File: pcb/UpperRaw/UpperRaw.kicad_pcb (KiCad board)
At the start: 2 copper layers, 52 x 63 mm, 20 parts, among them J1 Conn_01x04, SW100 SW_DPDT_x2, SW101 SW_DPDT_x2, SW102 SW_SPDT, SW103 SW_SPDT

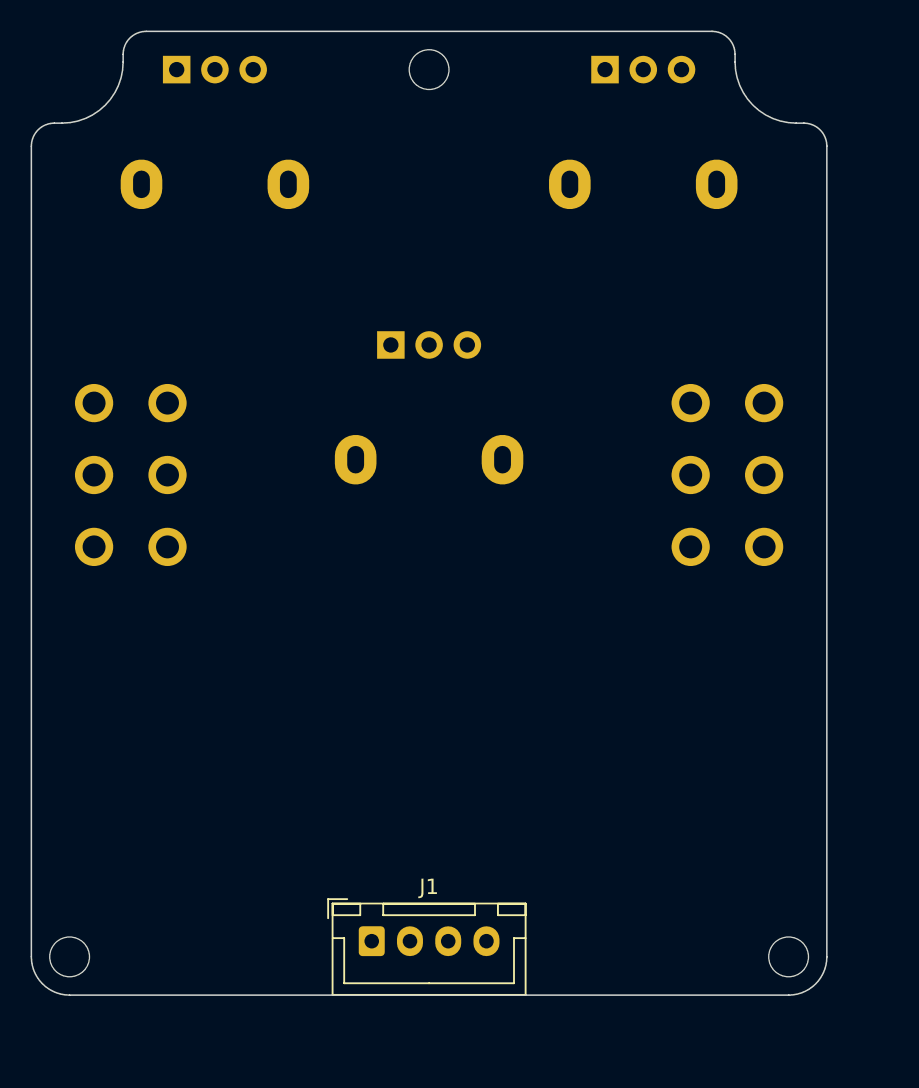
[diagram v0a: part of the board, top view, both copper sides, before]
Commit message: [UpperRaw] swap mounting holes for M3 ones
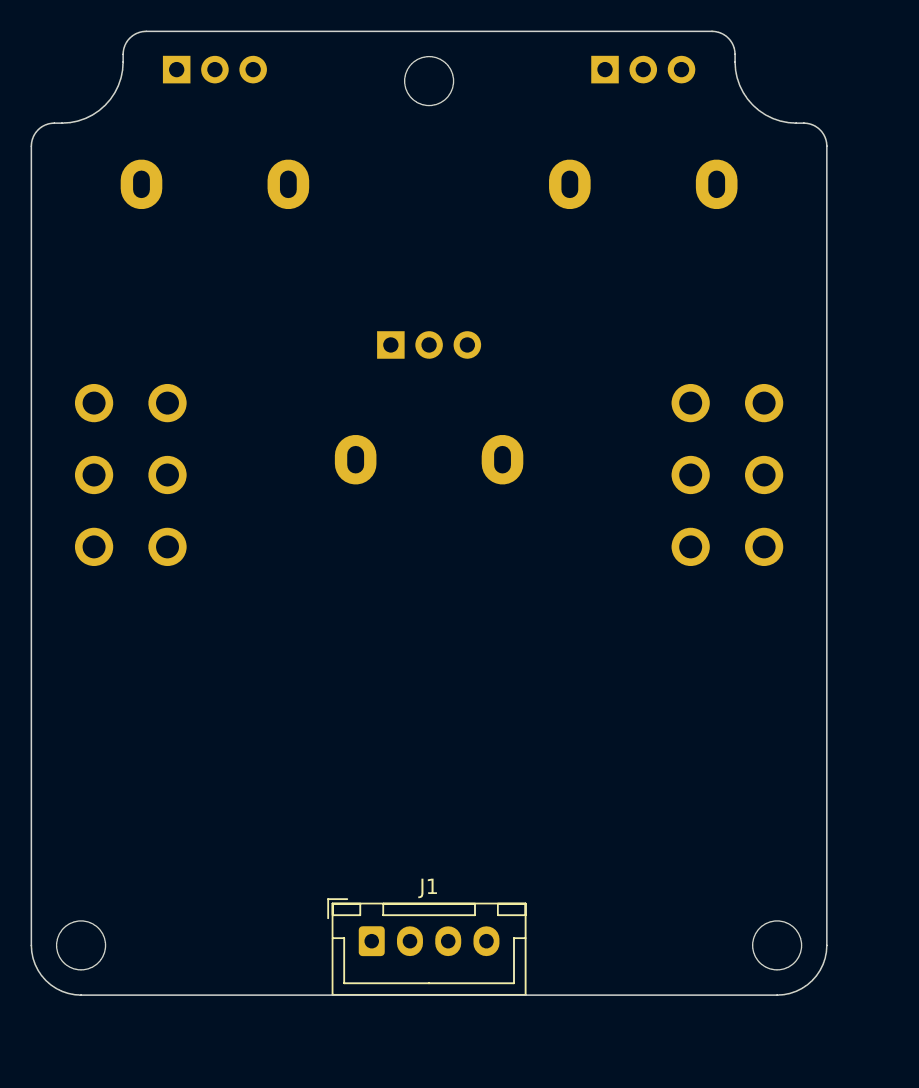
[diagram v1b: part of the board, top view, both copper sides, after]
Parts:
- removed the MK2 at (149.5, 70.0)
- removed the MK2 at (173.0, 128.0)
- removed the MK2 at (126.0, 128.0)
- added MK2: Mounting_Hole, MeineBib:EigenesMountingHole_3.2mm_M3_Small, F.Cu at (126.8, 127.2)
- added MK2: Mounting_Hole, MeineBib:EigenesMountingHole_3.2mm_M3_Small, F.Cu at (172.2, 127.2)
- added MK2: Mounting_Hole, MeineBib:EigenesMountingHole_3.2mm_M3_Small, F.Cu at (149.5, 70.8)
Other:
- outline, holes or cut-outs redrawn
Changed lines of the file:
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@@
+    )
+  )
+  (footprint "MeineBib:EigenesMountingHole_3.2mm_M3_Small" (layer "F.Cu")
+    (at 126.75 127.25)
+    (descr "Mounting Hole 2.7mm, no annular, M2.5")
+    (tags "mounting hole 2.7mm no annular m2.5")
+    (attr exclude_from_pos_files exclude_from_bom)
+    (fp_text reference "MK2" (at 0 -3.7) (layer "F.SilkS") hide
+      (effects (font (size 1 1) (thickness 0.15)))
+    )
+    (fp_text value "Mounting_Hole" (at 0 3.7) (layer "F.Fab")
+      (effects (font (size 1 1) (thickness 0.15)))
+    )
+    (fp_text user "${REFERENCE}" (at 0.3 0) (layer "F.Fab")
+      (effects (font (size 1 1) (thickness 0.15)))
+    )
+    (fp_circle (center 0 0) (end 3.1 0) (layer "Cmts.User") (width 0.15) (fill none))
+    (fp_circle (center 0 0) (end 3.1 0) (layer "F.CrtYd") (width 0.05) (fill none))
+    (pad "" np_thru_hole circle (at 0 0) (size 3.2 3.2) (drill 3.2) (layers F&B.Cu *.Mask)
+      (solder_mask_margin 1.65) (clearance 1.8))
+    (model "${MEINE_BIBS}/MeineBib.3dshapes/m3standoffs/M3x6-Screw.wrl"
+      (offset (xyz 0 0 0))
+      (scale (xyz 1 1 1))
+      (rotate (xyz 0 0 0))
+    )
+    (model "${MEINE_BIBS}/MeineBib.3dshapes/m3standoffs/M3x5x10-Spacer.wrl"
+      (offset (xyz 0 0 -11.6))
+      (scale (xyz 1 1 1))
+      (rotate (xyz 0 0 0))
     )
   )
@@
     )
   )
-  (footprint "MeineBib:EigenesMountingHole_2.6mm_M2.5_Small" (layer "F.Cu")
-    (at 149.5 70)
+  (footprint "MeineBib:EigenesMountingHole_3.2mm_M3_Small" (layer "F.Cu")
+    (at 172.25 127.25)
     (descr "Mounting Hole 2.7mm, no annular, M2.5")
     (tags "mounting hole 2.7mm no annular m2.5")
-    (attr board_only exclude_from_pos_files exclude_from_bom)
+    (attr exclude_from_pos_files exclude_from_bom)
     (fp_text reference "MK2" (at 0 -3.7) (layer "F.SilkS") hide
       (effects (font (size 1 1) (thickness 0.15)))
     )
-    (fp_text value "Mounting_Hole" (at 0 -0.13) (layer "F.Fab")
+    (fp_text value "Mounting_Hole" (at 0 3.7) (layer "F.Fab")
       (effects (font (size 1 1) (thickness 0.15)))
     )
@@
       (effects (font (size 1 1) (thickness 0.15)))
     )
-    (fp_circle (center 0 0) (end 2.5 0) (layer "Cmts.User") (width 0.15) (fill none))
-    (fp_circle (center 0 0) (end 2.5 0) (layer "F.CrtYd") (width 0.05) (fill none))
-    (pad "" np_thru_hole circle (at 0 0) (size 2.6 2.6) (drill 2.6) (layers F&B.Cu *.Mask)
-      (solder_mask_margin 1.25) (clearance 1.25))
+    (fp_circle (center 0 0) (end 3.1 0) (layer "Cmts.User") (width 0.15) (fill none))
+    (fp_circle (center 0 0) (end 3.1 0) (layer "F.CrtYd") (width 0.05) (fill none))
+    (pad "" np_thru_hole circle (at 0 0) (size 3.2 3.2) (drill 3.2) (layers F&B.Cu *.Mask)
+      (solder_mask_margin 1.65) (clearance 1.8))
+    (model "${MEINE_BIBS}/MeineBib.3dshapes/m3standoffs/M3x6-Screw.wrl"
+      (offset (xyz 0 0 0))
+      (scale (xyz 1 1 1))
+      (rotate (xyz 0 0 0))
+    )
+    (model "${MEINE_BIBS}/MeineBib.3dshapes/m3standoffs/M3x5x10-Spacer.wrl"
+      (offset (xyz 0 0 -11.6))
+      (scale (xyz 1 1 1))
+      (rotate (xyz 0 0 0))
+    )
   )
   (footprint "Resistor_SMD:R_0603_1608Metric" (layer "F.Cu")
@@
     )
   )
-  (footprint "MeineBib:EigenesMountingHole_2.6mm_M2.5_Small" (layer "F.Cu")
-    (at 173 128)
-    (descr "Mounting Hole 2.7mm, no annular, M2.5")
-    (tags "mounting hole 2.7mm no annular m2.5")
-    (attr board_only exclude_from_pos_files exclude_from_bom)
-    (fp_text reference "MK2" (at 0 -3.7) (layer "F.SilkS") hide
-      (effects (font (size 1 1) (thickness 0.15)))
-    )
-    (fp_text value "Mounting_Hole" (at 0 -0.13) (layer "F.Fab")
-      (effects (font (size 1 1) (thickness 0.15)))
-    )
-    (fp_text user "${REFERENCE}" (at 0.3 0) (layer "F.Fab")
-      (effects (font (size 1 1) (thickness 0.15)))
-    )
-    (fp_circle (center 0 0) (end 2.5 0) (layer "Cmts.User") (width 0.15) (fill none))
-    (fp_circle (center 0 0) (end 2.5 0) (layer "F.CrtYd") (width 0.05) (fill none))
-    (pad "" np_thru_hole circle (at 0 0) (size 2.6 2.6) (drill 2.6) (layers F&B.Cu *.Mask)
-      (solder_mask_margin 1.25) (clearance 1.25))
-  )
-  (footprint "MeineBib:EigenesMountingHole_2.6mm_M2.5_Small" (layer "F.Cu")
-    (at 126 128)
-    (descr "Mounting Hole 2.7mm, no annular, M2.5")
-    (tags "mounting hole 2.7mm no annular m2.5")
-    (attr board_only exclude_from_pos_files exclude_from_bom)
-    (fp_text reference "MK2" (at 0 -3.7) (layer "F.SilkS") hide
-      (effects (font (size 1 1) (thickness 0.15)))
-    )
-    (fp_text value "Mounting_Hole" (at 0 -0.078) (layer "F.Fab")
-      (effects (font (size 1 1) (thickness 0.15)))
-    )
-    (fp_text user "${REFERENCE}" (at 0.3 0) (layer "F.Fab")
-      (effects (font (size 1 1) (thickness 0.15)))
-    )
-    (fp_circle (center 0 0) (end 2.5 0) (layer "Cmts.User") (width 0.15) (fill none))
-    (fp_circle (center 0 0) (end 2.5 0) (layer "F.CrtYd") (width 0.05) (fill none))
-    (pad "" np_thru_hole circle (at 0 0) (size 2.6 2.6) (drill 2.6) (layers F&B.Cu *.Mask)
-      (solder_mask_margin 1.25) (clearance 1.25))
-  )
   (footprint "Resistor_SMD:R_0603_1608Metric" (layer "F.Cu")
     (at 251.1 157.776)
@@
     (model "${KICAD6_3DMODEL_DIR}/Resistor_SMD.3dshapes/R_0603_1608Metric.wrl"
       (offset (xyz 0 0 0))
+      (scale (xyz 1 1 1))
+      (rotate (xyz 0 0 0))
+    )
+  )
+  (footprint "MeineBib:EigenesMountingHole_3.2mm_M3_Small" (layer "F.Cu")
+    (at 149.5 70.75)
+    (descr "Mounting Hole 2.7mm, no annular, M2.5")
+    (tags "mounting hole 2.7mm no annular m2.5")
+    (attr exclude_from_pos_files exclude_from_bom)
+    (fp_text reference "MK2" (at 0 -3.7) (layer "F.SilkS") hide
+      (effects (font (size 1 1) (thickness 0.15)))
+    )
+    (fp_text value "Mounting_Hole" (at 0 3.7) (layer "F.Fab")
+      (effects (font (size 1 1) (thickness 0.15)))
+    )
+    (fp_text user "${REFERENCE}" (at 0.3 0) (layer "F.Fab")
+      (effects (font (size 1 1) (thickness 0.15)))
+    )
+    (fp_circle (center 0 0) (end 3.1 0) (layer "Cmts.User") (width 0.15) (fill none))
+    (fp_circle (center 0 0) (end 3.1 0) (layer "F.CrtYd") (width 0.05) (fill none))
+    (pad "" np_thru_hole circle (at 0 0) (size 3.2 3.2) (drill 3.2) (layers F&B.Cu *.Mask)
+      (solder_mask_margin 1.65) (clearance 1.8))
+    (model "${MEINE_BIBS}/MeineBib.3dshapes/m3standoffs/M3x6-Screw.wrl"
+      (offset (xyz 0 0 0))
+      (scale (xyz 1 1 1))
+      (rotate (xyz 0 0 0))
+    )
+    (model "${MEINE_BIBS}/MeineBib.3dshapes/m3standoffs/M3x5x10-Spacer.wrl"
+      (offset (xyz 0 0 -11.6))
       (scale (xyz 1 1 1))
       (rotate (xyz 0 0 0))
@@
   (gr_arc (start 129.5 69.5) (mid 128.328427 72.328427) (end 125.5 73.5) (layer "Edge.Cuts") (width 0.1))
   (gr_line (start 174 73.5) (end 173.5 73.5) (layer "Edge.Cuts") (width 0.1))
-  (gr_line (start 175.5 75) (end 175.5 128) (layer "Edge.Cuts") (width 0.1))
+  (gr_line (start 175.5 75) (end 175.5 127.25) (layer "Edge.Cuts") (width 0.1))
+  (gr_arc (start 126.75 130.5) (mid 124.451903 129.548097) (end 123.5 127.25) (layer "Edge.Cuts") (width 0.1))
   (gr_arc (start 173.5 73.5) (mid 170.671573 72.328427) (end 169.5 69.5) (layer "Edge.Cuts") (width 0.1))
-  (gr_line (start 123.5 75) (end 123.5 128) (layer "Edge.Cuts") (width 0.1))
+  (gr_line (start 123.5 75) (end 123.5 127.25) (layer "Edge.Cuts") (width 0.1))
   (gr_arc (start 123.5 75) (mid 123.93934 73.93934) (end 125 73.5) (layer "Edge.Cuts") (width 0.1))
-  (gr_line (start 126 130.5) (end 173 130.5) (layer "Edge.Cuts") (width 0.1))
-  (gr_arc (start 126 130.5) (mid 124.232233 129.767767) (end 123.5 128) (layer "Edge.Cuts") (width 0.1))
+  (gr_line (start 126.75 130.5) (end 172.25 130.5) (layer "Edge.Cuts") (width 0.1))
+  (gr_arc (start 175.5 127.25) (mid 174.548097 129.548097) (end 172.25 130.5) (layer "Edge.Cuts") (width 0.1))
   (gr_arc (start 129.5 69) (mid 129.93934 67.93934) (end 131 67.5) (layer "Edge.Cuts") (width 0.1))
   (gr_arc (start 168 67.5) (mid 169.06066 67.93934) (end 169.5 69) (layer "Edge.Cuts") (width 0.1))
-  (gr_arc (start 175.5 128) (mid 174.767767 129.767767) (end 173 130.5) (layer "Edge.Cuts") (width 0.1))
   (gr_line (start 169.5 69) (end 169.5 69.5) (layer "Edge.Cuts") (width 0.1))
   (gr_line (start 131 67.5) (end 168 67.5) (layer "Edge.Cuts") (width 0.1))

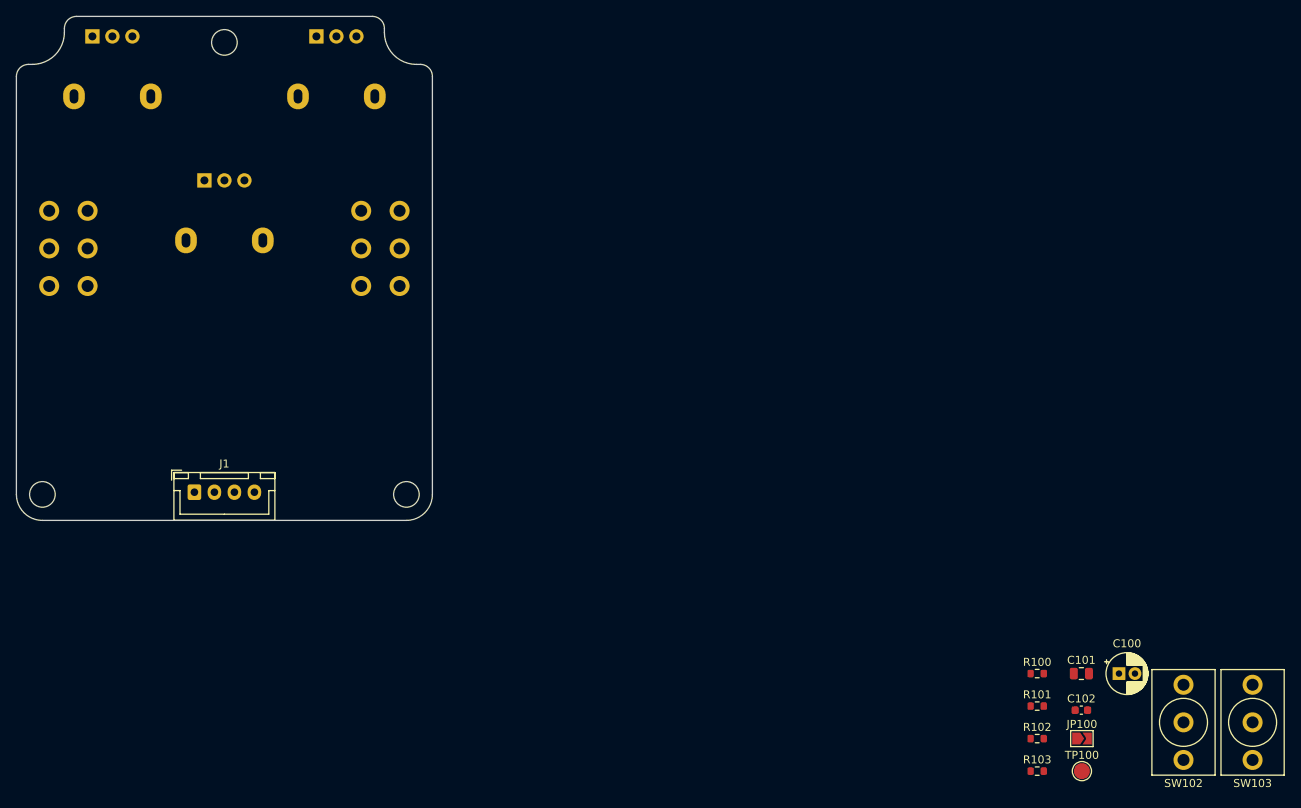
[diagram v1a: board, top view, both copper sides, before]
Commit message: [UpperRaw] Create template with logos, tooling holes etc.
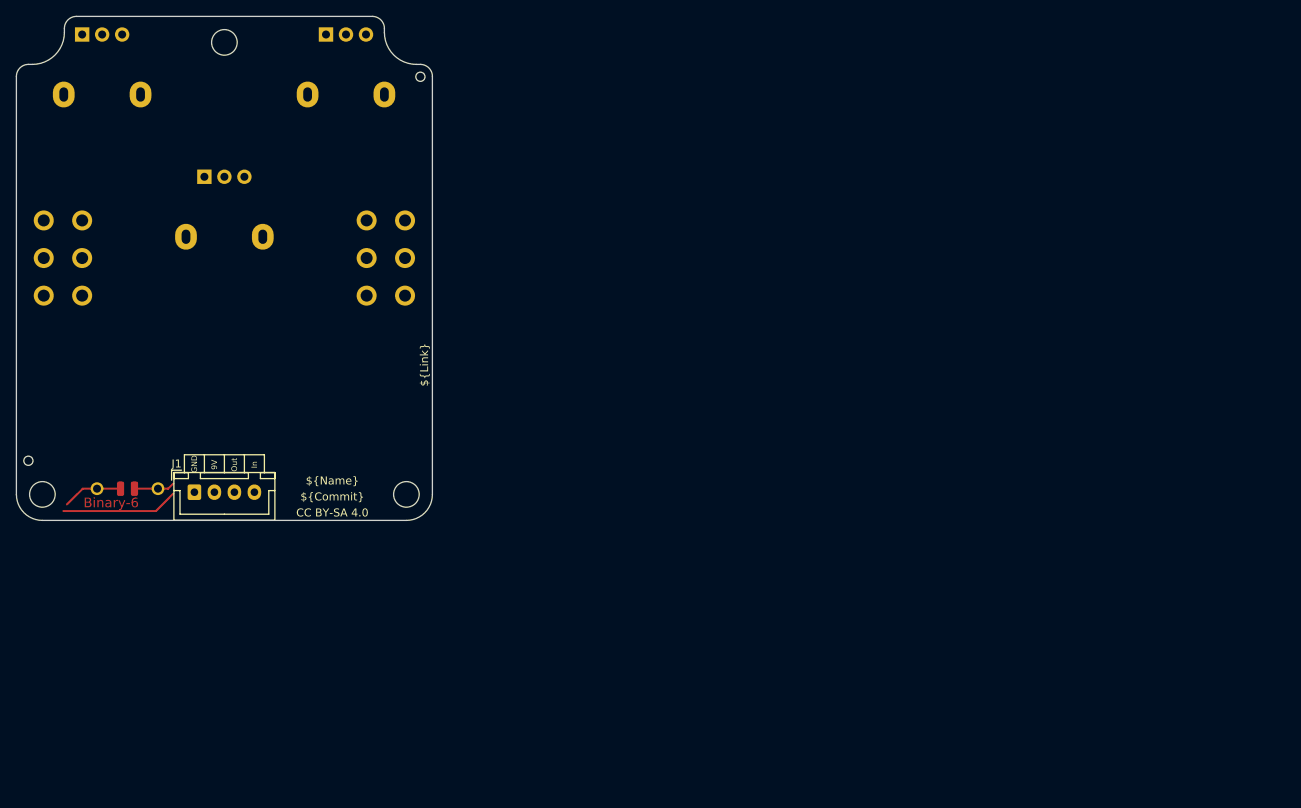
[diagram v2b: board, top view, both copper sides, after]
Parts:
- removed C100: 100uF, Capacitor_THT:CP_Radial_D5.0mm_P2.00mm
- removed C101: 10uF, Capacitor_SMD:C_0805_2012Metric
- removed C102: 220nF, Capacitor_SMD:C_0603_1608Metric
- removed JP100: Jmp, Jumper:SolderJumper-2_P1.3mm_Open_TrianglePad1.0x1.5mm
- removed R100: 1M, Resistor_SMD:R_0603_1608Metric
- removed R101: 2M2, Resistor_SMD:R_0603_1608Metric
- removed R102: 390R, Resistor_SMD:R_0603_1608Metric
- removed R103: 2k2, Resistor_SMD:R_0603_1608Metric
- removed SW102, SW103: SW_SPDT, MeineBib:Switch_toggle_SPDT_Print
- removed TP100: TP, TestPoint:TestPoint_Pad_D2.0mm
- added H7: Symbol_Binary6, MeineBib:Binary_6_v0.1_tiny_silk, F.Cu at (137.4, 127.5)
- added REF**: JLC_Toolinghole, MeineBib:JLC_Toolinghole, F.Cu at (125.0, 123.0)
- added REF**: JLC_Toolinghole, MeineBib:JLC_Toolinghole, F.Cu at (174.0, 75.0)
- MK2 (x3): value Mounting_Hole -> Mounting_Hole_M3
- moved SW100 1.38 mm to (129.3, 97.7)
- moved SW101 1.38 mm to (169.7, 97.7)
- moved RV101 1.30 mm to (131.7, 69.8)
- moved RV102 1.22 mm to (162.2, 69.8)
- moved RV100 0.45 mm to (147.0, 87.5)
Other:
- board text added: "${Commit}"
- board text added: "${Link}"
- board text added: "${Name}"
- board text added: "9V"
- board text added: "CC BY-SA 4.0"
- board text added: "GND"
- board text added: "In"
- board text added: "JLCJLCJLCJLC"
- board text added: "Out"
- board text removed: "Imports from Copypasta grave"
